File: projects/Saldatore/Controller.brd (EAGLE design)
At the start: 50.8 x 33 mm, 20 parts, among them U1 ATTINY85-P

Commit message: in lavoro saldatore.
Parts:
- R4: value 47-2W -> 120-5W
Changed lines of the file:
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@@
 <drawing>
 <settings>
-<setting alwaysvectorfont="yes"/>
+<setting alwaysvectorfont="no"/>
 <setting verticaltext="up"/>
 </settings>
@@
 <attribute name="VALUE" x="32.29" y="22.99" size="1.27" layer="27" rot="R90"/>
 </element>
-<element name="R4" library="rcl" library_urn="urn:adsk.eagle:library:334" package="0204/7" package3d_urn="urn:adsk.eagle:package:23498/2" value="47-2W" x="36.83" y="44.45" smashed="yes" rot="R270">
+<element name="R4" library="rcl" library_urn="urn:adsk.eagle:library:334" package="0204/7" package3d_urn="urn:adsk.eagle:package:23498/2" value="120-5W" x="36.83" y="44.45" smashed="yes" rot="R270">
 <attribute name="NAME" x="38.1254" y="46.99" size="0.9906" layer="25" ratio="10" rot="R270"/>
 <attribute name="POPULARITY" value="79" x="-8.89" y="6.35" size="1.778" layer="27" rot="R270" display="off"/>

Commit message: aggiornato saldatore.
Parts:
- removed D2: 5v1-1W, diode_MOD:DO41Z10
- removed R4: 120-5W, rcl:0204/7
- added C1: 0.1u, rcl:C025-025X050
- added C2: 1u, rcl:C025-025X050
- added LM317: (no value), v-reg:317TS
- added R10: 240, rcl:0204/7
- added R12: 1k, rcl:RTRIM64W
- R1: value 270 -> 220
- R8: value 10K -> 1k
- renumbered LM358 to LM258
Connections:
- new net N$67: LM317.1, R10.1, R12.1
- net 24V: now also C1.2, LM317.3; no longer R4.2
- net GND: now also C1.1, C2.1, R12.2, R12.3; no longer D2.A
- net VCC: now also C2.2, LM317.2, R10.2; no longer D2.C, R4.1
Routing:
- net VCC: track 66.2 -> 109.2 mm
- net N$67: track 0.00 -> 30.5 mm
- net 24V: track 33.1 -> 43.2 mm
- net GND: track 105.5 -> 110.6 mm
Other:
- board outline removed

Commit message: in lavoro immagine scheda controller.
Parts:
- LM258: value LM358N -> LM258N

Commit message: aggiornato controller
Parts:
- removed LED1: (no value), led:LED3MM
- added LED: (no value), jumper:JP1
- U1: value ATTINY85-P -> ATTINY85
- renumbered JP1 to RST, PROGRAMMER to PROG, SOLDERING to SOLD, TRIMM_100K to T_100K
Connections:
- net GND: now also LED.2; no longer LED1.K
- net N$61: now also LED.1; no longer LED1.A
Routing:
- net GND: track 110.6 -> 111.8 mm
- net N$61: track 3.81 -> 2.54 mm

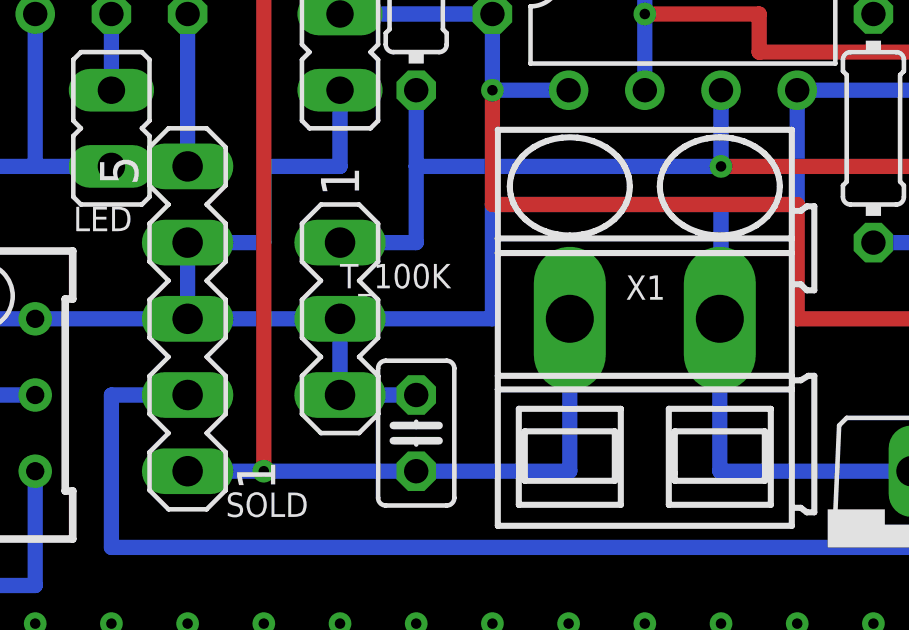
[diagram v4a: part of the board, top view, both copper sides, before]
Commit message: aggiornata configurazione potenziometro di comando.
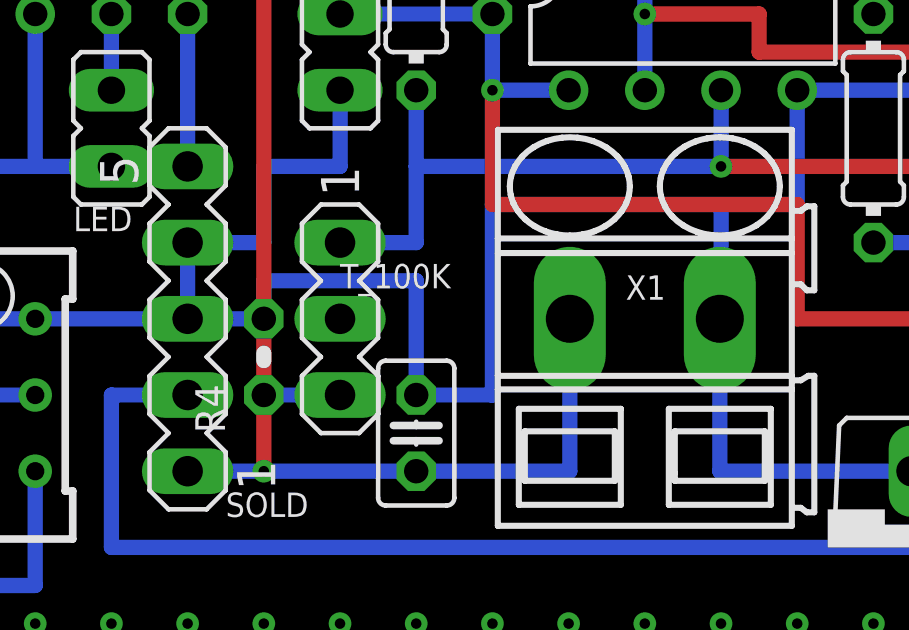
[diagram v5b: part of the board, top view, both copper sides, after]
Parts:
- added R4: 10K, rcl:0204V
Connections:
- new net N$72: R4.1, T_100K.3
- net ADC_CMD: now also T_100K.2
- net GND: now also R4.2; no longer T_100K.2, T_100K.3
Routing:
- net N$72: track 0.00 -> 2.54 mm
- net GND: track 111.8 -> 114.4 mm
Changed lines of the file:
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@@
 <?xml version="1.0" encoding="utf-8"?>
 <!DOCTYPE eagle SYSTEM "eagle.dtd">
-<eagle version="9.5.2">
+<eagle version="9.5.1">
 <drawing>
 <settings>
-<setting alwaysvectorfont="yes"/>
+<setting alwaysvectorfont="no"/>
 <setting verticaltext="up"/>
 </settings>
@@
 <attribute name="VALUE" x="28.829" y="39.37" size="1.27" layer="27" ratio="10" rot="R270"/>
 </element>
+<element name="R4" library="rcl" library_urn="urn:adsk.eagle:library:334" package="0204V" package3d_urn="urn:adsk.eagle:package:23495/1" value="10K" x="36.83" y="29.21" smashed="yes" rot="R90">
+<attribute name="NAME" x="35.5346" y="26.67" size="0.9906" layer="25" ratio="10" rot="R90"/>
+<attribute name="POPULARITY" value="11" x="36.83" y="29.21" size="1.778" layer="27" rot="R90" display="off"/>
+<attribute name="SPICEPREFIX" value="R" x="36.83" y="29.21" size="1.778" layer="27" rot="R90" display="off"/>
+<attribute name="VALUE" x="37.3126" y="27.5844" size="0.9906" layer="27" ratio="10" rot="R90"/>
+</element>
 </elements>
 <signals>
@@
 <contactref element="SOLD" pad="3"/>
 <contactref element="X1" pad="2"/>
-<contactref element="T_100K" pad="2"/>
-<contactref element="T_100K" pad="3"/>
 <contactref element="U1" pad="4"/>
 <wire x1="52.07" y1="34.29" x2="52.07" y2="30.48" width="0.508" layer="16"/>
 <wire x1="52.07" y1="30.48" x2="52.03" y2="30.48" width="0.508" layer="16"/>
-<wire x1="39.37" y1="30.48" x2="39.37" y2="27.94" width="0.508" layer="16"/>
 <wire x1="29.21" y1="30.48" x2="26.67" y2="30.48" width="0.508" layer="16"/>
 <contactref element="SOLD" pad="4"/>
@@
 <wire x1="54.61" y1="34.29" x2="52.07" y2="34.29" width="0.508" layer="16"/>
 <contactref element="RST" pad="2"/>
-<wire x1="34.29" y1="30.48" x2="39.37" y2="30.48" width="0.508" layer="16"/>
-<wire x1="39.37" y1="30.48" x2="44.45" y2="30.48" width="0.508" layer="16"/>
-<wire x1="44.45" y1="30.48" x2="44.45" y2="34.29" width="0.508" layer="16"/>
-<wire x1="44.45" y1="34.29" x2="52.07" y2="34.29" width="0.508" layer="16"/>
+<wire x1="52.07" y1="34.29" x2="44.45" y2="34.29" width="0.508" layer="16"/>
 <wire x1="34.29" y1="33.02" x2="36.83" y2="33.02" width="0.508" layer="16"/>
 <wire x1="36.83" y1="33.02" x2="36.83" y2="35.56" width="0.508" layer="16"/>
@@
 <wire x1="59.69" y1="40.64" x2="59.69" y2="45.72" width="0.508" layer="16"/>
 <wire x1="59.69" y1="45.72" x2="62.23" y2="45.72" width="0.508" layer="16"/>
-<wire x1="39.37" y1="27.94" x2="41.91" y2="27.94" width="0.508" layer="16"/>
 <wire x1="52.07" y1="48.26" x2="54.61" y2="48.26" width="0.508" layer="16"/>
 <wire x1="54.61" y1="48.26" x2="57.15" y2="48.26" width="0.508" layer="16"/>
@@
 <contactref element="LED" pad="2"/>
 <wire x1="31.75" y1="35.56" x2="29.21" y2="35.56" width="0.508" layer="16"/>
+<contactref element="R4" pad="2"/>
+<wire x1="34.29" y1="30.48" x2="36.83" y2="30.48" width="0.508" layer="16"/>
+<wire x1="44.45" y1="27.94" x2="41.91" y2="27.94" width="0.508" layer="16"/>
+<wire x1="44.45" y1="34.29" x2="44.45" y2="27.94" width="0.508" layer="16"/>
+<wire x1="36.83" y1="30.48" x2="36.83" y2="31.75" width="0.508" layer="16"/>
+<wire x1="36.83" y1="31.75" x2="41.91" y2="31.75" width="0.508" layer="16"/>
+<wire x1="41.91" y1="31.75" x2="41.91" y2="27.94" width="0.508" layer="16"/>
 </signal>
 <signal name="N$1">
@@
 <via x="52.07" y="35.56" extent="1-16" drill="0.35"/>
 <wire x1="52.07" y1="35.56" x2="62.23" y2="35.56" width="0.508" layer="1"/>
+<contactref element="T_100K" pad="2"/>
+<wire x1="39.37" y1="30.48" x2="39.37" y2="33.02" width="0" layer="19" extent="1-1"/>
 </signal>
 <signal name="ADC_TEMP">
@@
 <via x="67.31" y="50.8" extent="1-16" drill="0.35"/>
 </signal>
+<signal name="N$72">
+<contactref element="T_100K" pad="3"/>
+<contactref element="R4" pad="1"/>
+<wire x1="36.83" y1="27.94" x2="39.37" y2="27.94" width="0.508" layer="16"/>
+</signal>
 </signals>
